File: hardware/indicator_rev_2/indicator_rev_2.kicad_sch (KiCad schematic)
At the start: 23 parts, among them J2 Conn_01x04_Pin, U1 TCA6408ARSVR, U2 TLV70033DCKR

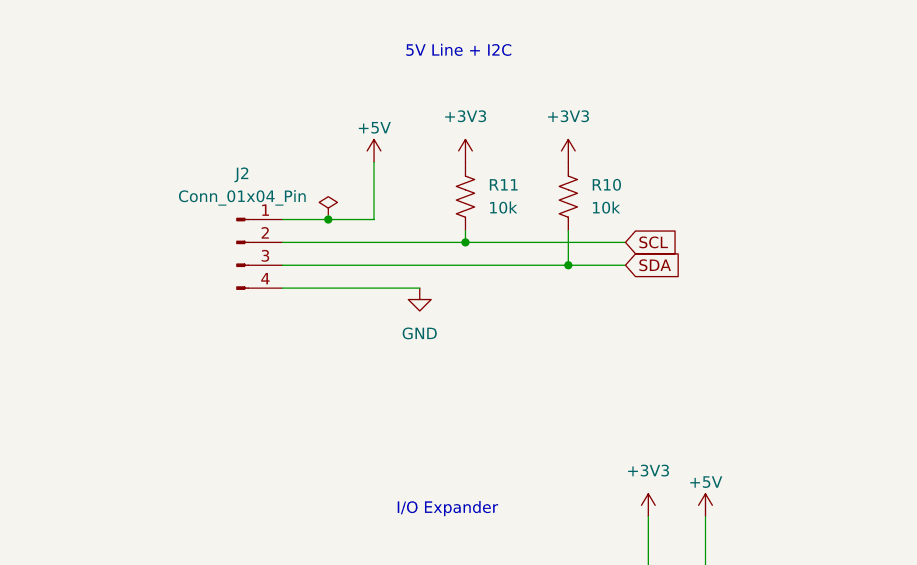
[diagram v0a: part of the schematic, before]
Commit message: modified i2c header and pushed connector
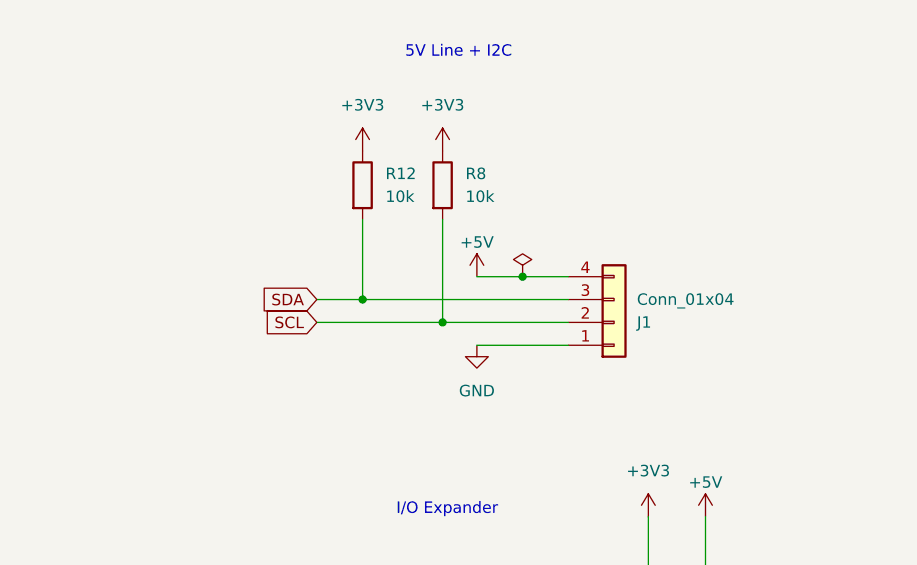
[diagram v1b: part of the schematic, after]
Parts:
- removed J2: Conn_01x04_Pin, Connector_JST:JST_XH_S4B-XH-A_1x04_P2.50mm_Horizontal, symbol Connector:Conn_01x04_Pin
- removed R10, R11: 10k, Resistor_SMD:R_0603_1608Metric, symbol Device:R_US
- added J1: Conn_01x04, Connector_JST:JST_XH_S4B-XH-A_1x04_P2.50mm_Horizontal, symbol Connector_Generic:Conn_01x04
- added R12, R8: 10k, Resistor_SMD:R_0603_1608Metric, symbol Device:R
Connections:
- net +3V3: now also R12.1, R8.1
- net +5V: now also J1.4 (Pin_4)
- net GND: now also J1.1 (Pin_1)
- net SCL: now also J1.2 (Pin_2), R8.2
- net SDA: now also J1.3 (Pin_3), R12.2
